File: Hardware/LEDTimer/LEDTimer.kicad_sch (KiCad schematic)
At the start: 36 parts, among them J2 LED, J3 PWR, SW1 SW_Push, SW2 SW_Push, SW3 SW_Push, SW4 SW_BAT, U1 AP7383-36WW7, U2 PIC16F1825, U3 Display_128x64_096_I2C, U4 BCR_421U_E6327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

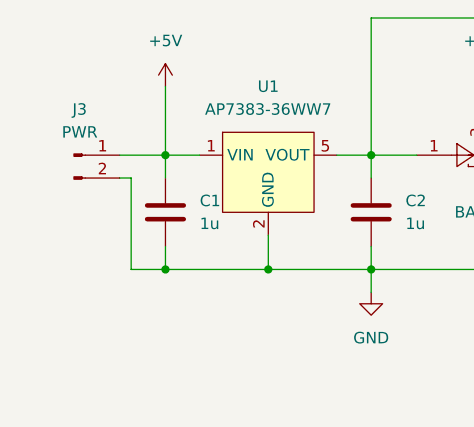
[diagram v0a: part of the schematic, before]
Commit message: PCB: flip the power input connector
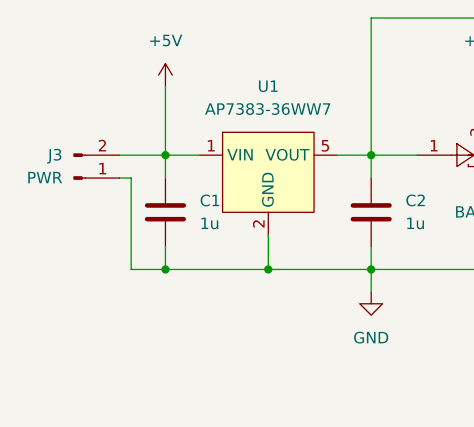
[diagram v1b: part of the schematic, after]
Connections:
- net +5V: now also J3.2 (Pin_2); no longer J3.1 (Pin_1)
- net GND: now also J3.1 (Pin_1); no longer J3.2 (Pin_2)
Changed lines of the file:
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@@
     (pin "3")
   )
-  (symbol (lib_id "Connector:Conn_01x02_Male") (at 20.32 41.91 0) (unit 1)
+  (symbol (lib_id "Connector:Conn_01x02_Male") (at 20.32 44.45 0) (mirror x) (unit 1)
     (in_bom yes) (on_board yes) (fields_autoplaced)
-    (property "Reference" "J3" (id 0) (at 20.955 36.83 0))
-    (property "Value" "PWR" (id 1) (at 20.955 39.37 0))
-    (property "Footprint" "Connector_PinHeader_2.54mm:PinHeader_1x02_P2.54mm_Horizontal" (id 2) (at 20.32 41.91 0)
+    (property "Reference" "J3" (id 0) (at 19.05 41.9099 0)
+      (effects (font (size 1.27 1.27)) (justify right))
+    )
+    (property "Value" "PWR" (id 1) (at 19.05 44.4499 0)
+      (effects (font (size 1.27 1.27)) (justify right))
+    )
+    (property "Footprint" "Connector_PinHeader_2.54mm:PinHeader_1x02_P2.54mm_Horizontal" (id 2) (at 20.32 44.45 0)
       (effects (font (size 1.27 1.27)) hide)
     )
-    (property "Datasheet" "~" (id 3) (at 20.32 41.91 0)
+    (property "Datasheet" "~" (id 3) (at 20.32 44.45 0)
       (effects (font (size 1.27 1.27)) hide)
     )

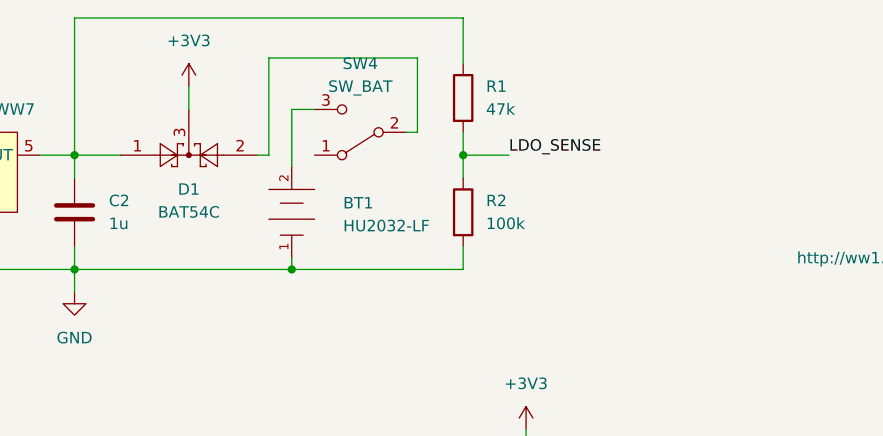
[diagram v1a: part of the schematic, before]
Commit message: PCB: re-purpose the switch as main power switch, add a transistor to LDO_SENSE for protection
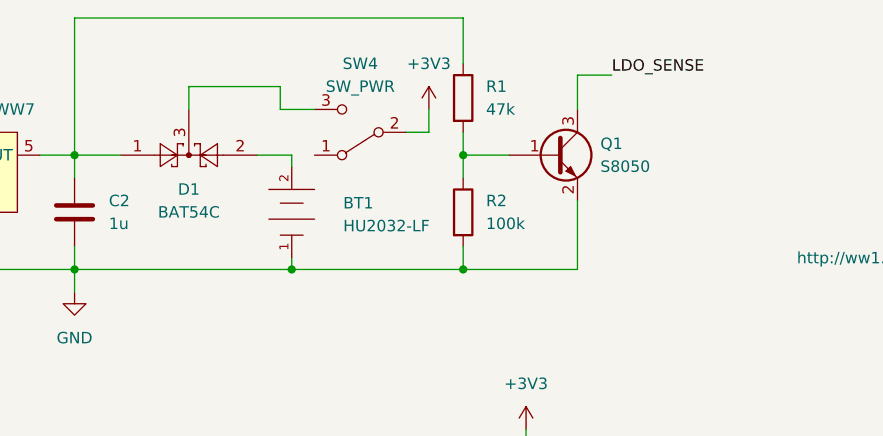
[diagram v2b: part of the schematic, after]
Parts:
- added Q1: S8050, Package_TO_SOT_SMD:SOT-23, symbol Device:Q_NPN_BEC
- SW4: value SW_BAT -> SW_PWR
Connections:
- net +3V3: now also SW4.2 (B); no longer D1.3
- net GND: now also Q1.2 (E)
- net LDO_SENSE: now also Q1.3 (C); no longer R1.2, R2.1
- net at BT1.2 (ANODE): now also D1.2; no longer SW4.3 (C)
- new net: Q1.1 (B), R1.2, R2.1
- new net: D1.3, SW4.3 (C)
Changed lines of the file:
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@@
   (junction (at 194.31 135.89) (diameter 0) (color 0 0 0 0)
   )
+  (junction (at 96.52 54.61) (diameter 0) (color 0 0 0 0)
+  )
   (junction (at 77.47 54.61) (diameter 0) (color 0 0 0 0)
   )
@@
     (stroke (width 0) (type default) (color 0 0 0 0))
   )
-  (wire (pts (xy 74.93 41.91) (xy 73.66 41.91))
+  (wire (pts (xy 73.66 41.91) (xy 77.47 41.91))
     (stroke (width 0) (type default) (color 0 0 0 0))
   )
@@
     (stroke (width 0) (type default) (color 0 0 0 0))
   )
-  (wire (pts (xy 80.01 36.83) (xy 77.47 36.83))
-    (stroke (width 0) (type default) (color 0 0 0 0))
-  )
   (wire (pts (xy 116.205 151.13) (xy 149.225 151.13))
     (stroke (width 0) (type default) (color 0 0 0 0))
@@
     (stroke (width 0) (type default) (color 0 0 0 0))
   )
-  (wire (pts (xy 91.44 31.115) (xy 74.93 31.115))
-    (stroke (width 0) (type default) (color 0 0 0 0))
-  )
   (wire (pts (xy 132.08 76.835) (xy 132.08 83.185))
     (stroke (width 0) (type default) (color 0 0 0 0))
@@
     (stroke (width 0) (type default) (color 0 0 0 0))
   )
-  (wire (pts (xy 77.47 36.83) (xy 77.47 43.18))
-    (stroke (width 0) (type default) (color 0 0 0 0))
-  )
   (wire (pts (xy 88.9 111.76) (xy 86.995 111.76))
     (stroke (width 0) (type default) (color 0 0 0 0))
@@
     (stroke (width 0) (type default) (color 0 0 0 0))
   )
-  (wire (pts (xy 91.44 39.37) (xy 91.44 31.115))
-    (stroke (width 0) (type default) (color 0 0 0 0))
-  )
   (wire (pts (xy 164.465 101.6) (xy 167.005 101.6))
     (stroke (width 0) (type default) (color 0 0 0 0))
@@
     (stroke (width 0) (type default) (color 0 0 0 0))
   )
+  (wire (pts (xy 66.04 34.29) (xy 76.2 34.29))
+    (stroke (width 0) (type default) (color 0 0 0 0))
+  )
   (wire (pts (xy 53.34 41.91) (xy 58.42 41.91))
     (stroke (width 0) (type default) (color 0 0 0 0))
@@
     (stroke (width 0) (type default) (color 0 0 0 0))
   )
+  (wire (pts (xy 109.22 36.83) (xy 109.22 33.02))
+    (stroke (width 0) (type default) (color 0 0 0 0))
+  )
+  (wire (pts (xy 92.71 39.37) (xy 92.71 36.83))
+    (stroke (width 0) (type default) (color 0 0 0 0))
+  )
   (wire (pts (xy 113.665 138.43) (xy 116.205 138.43))
     (stroke (width 0) (type default) (color 0 0 0 0))
@@
     (stroke (width 0) (type default) (color 0 0 0 0))
   )
+  (wire (pts (xy 76.2 36.83) (xy 80.01 36.83))
+    (stroke (width 0) (type default) (color 0 0 0 0))
+  )
   (wire (pts (xy 187.325 85.725) (xy 187.325 111.76))
     (stroke (width 0) (type default) (color 0 0 0 0))
   )
-  (wire (pts (xy 74.93 31.115) (xy 74.93 41.91))
+  (wire (pts (xy 109.22 33.02) (xy 113.03 33.02))
     (stroke (width 0) (type default) (color 0 0 0 0))
   )
@@
     (stroke (width 0) (type default) (color 0 0 0 0))
   )
+  (wire (pts (xy 90.17 39.37) (xy 92.71 39.37))
+    (stroke (width 0) (type default) (color 0 0 0 0))
+  )
   (wire (pts (xy 164.465 104.14) (xy 171.45 104.14))
     (stroke (width 0) (type default) (color 0 0 0 0))
@@
     (stroke (width 0) (type default) (color 0 0 0 0))
   )
+  (wire (pts (xy 77.47 41.91) (xy 77.47 43.18))
+    (stroke (width 0) (type default) (color 0 0 0 0))
+  )
   (wire (pts (xy 193.04 140.97) (xy 194.31 140.97))
     (stroke (width 0) (type default) (color 0 0 0 0))
   )
-  (wire (pts (xy 90.17 39.37) (xy 91.44 39.37))
-    (stroke (width 0) (type default) (color 0 0 0 0))
-  )
   (wire (pts (xy 103.505 76.835) (xy 132.08 76.835))
     (stroke (width 0) (type default) (color 0 0 0 0))
@@
     (stroke (width 0) (type default) (color 0 0 0 0))
   )
+  (wire (pts (xy 109.22 46.99) (xy 109.22 54.61))
+    (stroke (width 0) (type default) (color 0 0 0 0))
+  )
   (wire (pts (xy 173.99 106.68) (xy 173.99 98.425))
     (stroke (width 0) (type default) (color 0 0 0 0))
@@
     (stroke (width 0) (type default) (color 0 0 0 0))
   )
+  (wire (pts (xy 76.2 34.29) (xy 76.2 36.83))
+    (stroke (width 0) (type default) (color 0 0 0 0))
+  )
   (wire (pts (xy 133.985 106.68) (xy 116.205 106.68))
     (stroke (width 0) (type default) (color 0 0 0 0))
@@
   )
   (wire (pts (xy 235.585 102.235) (xy 182.245 102.235))
+    (stroke (width 0) (type default) (color 0 0 0 0))
+  )
+  (wire (pts (xy 109.22 54.61) (xy 96.52 54.61))
     (stroke (width 0) (type default) (color 0 0 0 0))
   )
@@
     (effects (font (size 1.27 1.27)) (justify left bottom))
   )
-  (label "LDO_SENSE" (at 101.6 41.91 0)
+  (label "LDO_SENSE" (at 113.03 33.02 0)
     (effects (font (size 1.27 1.27)) (justify left bottom))
   )
@@
     (pin "2")
     (pin "5")
+  )
+  (symbol (lib_id "Device:Q_NPN_BEC") (at 106.68 41.91 0) (unit 1)
+    (in_bom yes) (on_board yes) (fields_autoplaced)
+    (property "Reference" "Q1" (id 0) (at 111.76 40.6399 0)
+      (effects (font (size 1.27 1.27)) (justify left))
+    )
+    (property "Value" "S8050" (id 1) (at 111.76 43.1799 0)
+      (effects (font (size 1.27 1.27)) (justify left))
+    )
+    (property "Footprint" "Package_TO_SOT_SMD:SOT-23" (id 2) (at 111.76 39.37 0)
+      (effects (font (size 1.27 1.27)) hide)
+    )
+    (property "Datasheet" "https://datasheet.lcsc.com/lcsc/1811101032_HT-Shenzhen-Jinyu-Semicon-S8050_C259988.pdf" (id 3) (at 106.68 41.91 0)
+      (effects (font (size 1.27 1.27)) hide)
+    )
+    (pin "1")
+    (pin "2")
+    (pin "3")
   )
   (symbol (lib_id "Device:R") (at 189.865 81.915 0) (unit 1)
@@
     (pin "1")
   )
-  (symbol (lib_id "power:+3V3") (at 66.04 34.29 0) (unit 1)
-    (in_bom yes) (on_board yes) (fields_autoplaced)
-    (property "Reference" "#PWR03" (id 0) (at 66.04 38.1 0)
-      (effects (font (size 1.27 1.27)) hide)
-    )
-    (property "Value" "+3V3" (id 1) (at 66.04 29.21 0))
-    (property "Footprint" "" (id 2) (at 66.04 34.29 0)
-      (effects (font (size 1.27 1.27)) hide)
-    )
-    (property "Datasheet" "" (id 3) (at 66.04 34.29 0)
+  (symbol (lib_id "power:+3V3") (at 92.71 36.83 0) (unit 1)
+    (in_bom yes) (on_board yes) (fields_autoplaced)
+    (property "Reference" "#PWR03" (id 0) (at 92.71 40.64 0)
+      (effects (font (size 1.27 1.27)) hide)
+    )
+    (property "Value" "+3V3" (id 1) (at 92.71 31.75 0))
+    (property "Footprint" "" (id 2) (at 92.71 36.83 0)
+      (effects (font (size 1.27 1.27)) hide)
+    )
+    (property "Datasheet" "" (id 3) (at 92.71 36.83 0)
       (effects (font (size 1.27 1.27)) hide)
     )
@@
     (in_bom yes) (on_board yes) (fields_autoplaced)
     (property "Reference" "SW4" (id 0) (at 85.09 31.75 0))
-    (property "Value" "SW_BAT" (id 1) (at 85.09 34.29 0))
+    (property "Value" "SW_PWR" (id 1) (at 85.09 34.29 0))
     (property "Footprint" "SPDT Switch:1825232-1" (id 2) (at 85.09 39.37 0)
       (effects (font (size 1.27 1.27)) hide)
@@
       (reference "JP2") (unit 1) (value "OLED2") (footprint "Jumper:SolderJumper-3_P1.3mm_Open_RoundedPad1.0x1.5mm")
     )
+    (path "/8ecc4707-fb83-41b7-ab7c-f7012336c37e"
+      (reference "Q1") (unit 1) (value "S8050") (footprint "Package_TO_SOT_SMD:SOT-23")
+    )
     (path "/c5745adf-2a60-4943-991a-b58822c9fa8c"
       (reference "R1") (unit 1) (value "47k") (footprint "Resistor_SMD:R_0805_2012Metric_Pad1.20x1.40mm_HandSolder")
@@
     )
     (path "/e49a9939-e5f7-4dfe-8005-f25d0240725f"
-      (reference "SW4") (unit 1) (value "SW_BAT") (footprint "SPDT Switch:1825232-1")
+      (reference "SW4") (unit 1) (value "SW_PWR") (footprint "SPDT Switch:1825232-1")
     )
     (path "/da811b11-3f5c-4085-9312-63fa595b7c79"

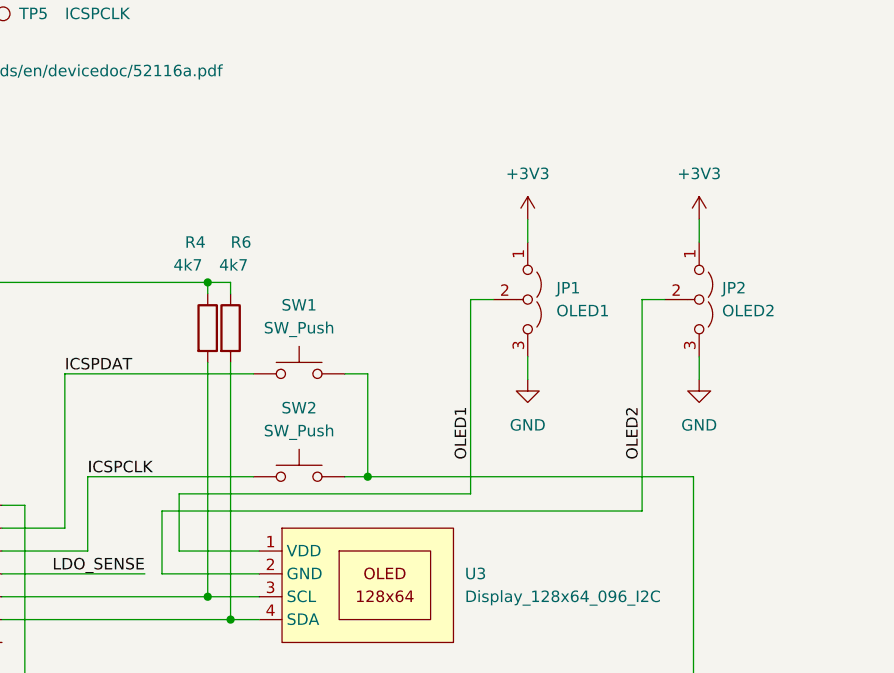
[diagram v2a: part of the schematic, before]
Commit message: PCB: add interactive BOM
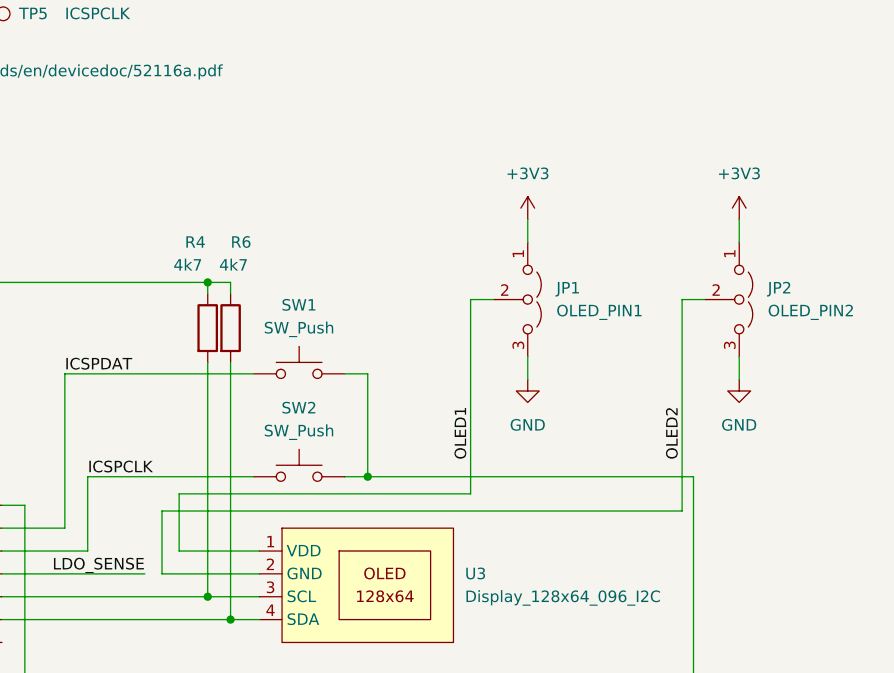
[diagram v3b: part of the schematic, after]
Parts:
- JP1: value OLED1 -> OLED_PIN1
- JP2: value OLED2 -> OLED_PIN2
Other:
- moved on the sheet: JP2
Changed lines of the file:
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@@
     (stroke (width 0) (type default) (color 0 0 0 0))
   )
-  (wire (pts (xy 235.585 78.74) (xy 235.585 102.235))
+  (wire (pts (xy 240.03 78.74) (xy 240.03 102.235))
     (stroke (width 0) (type default) (color 0 0 0 0))
   )
@@
     (stroke (width 0) (type default) (color 0 0 0 0))
   )
-  (wire (pts (xy 238.125 78.74) (xy 235.585 78.74))
+  (wire (pts (xy 242.57 78.74) (xy 240.03 78.74))
     (stroke (width 0) (type default) (color 0 0 0 0))
   )
@@
     (stroke (width 0) (type default) (color 0 0 0 0))
   )
-  (wire (pts (xy 241.935 85.09) (xy 241.935 87.63))
+  (wire (pts (xy 246.38 85.09) (xy 246.38 87.63))
     (stroke (width 0) (type default) (color 0 0 0 0))
   )
@@
     (stroke (width 0) (type default) (color 0 0 0 0))
   )
-  (wire (pts (xy 241.935 69.85) (xy 241.935 72.39))
+  (wire (pts (xy 246.38 69.85) (xy 246.38 72.39))
     (stroke (width 0) (type default) (color 0 0 0 0))
   )
@@
     (stroke (width 0) (type default) (color 0 0 0 0))
   )
-  (wire (pts (xy 235.585 102.235) (xy 182.245 102.235))
+  (wire (pts (xy 240.03 102.235) (xy 182.245 102.235))
     (stroke (width 0) (type default) (color 0 0 0 0))
   )
@@
     (effects (font (size 1.27 1.27)) (justify left bottom))
   )
-  (label "OLED2" (at 235.585 96.52 90)
+  (label "OLED2" (at 240.03 96.52 90)
     (effects (font (size 1.27 1.27)) (justify left bottom))
   )
@@
     )
   )
-  (symbol (lib_id "Jumper:Jumper_3_Open") (at 241.935 78.74 270) (unit 1)
-    (in_bom yes) (on_board yes) (fields_autoplaced)
-    (property "Reference" "JP2" (id 0) (at 244.475 77.4699 90)
-      (effects (font (size 1.27 1.27)) (justify left))
-    )
-    (property "Value" "OLED2" (id 1) (at 244.475 80.0099 90)
-      (effects (font (size 1.27 1.27)) (justify left))
-    )
-    (property "Footprint" "Jumper:SolderJumper-3_P1.3mm_Open_RoundedPad1.0x1.5mm" (id 2) (at 241.935 78.74 0)
-      (effects (font (size 1.27 1.27)) hide)
-    )
-    (property "Datasheet" "~" (id 3) (at 241.935 78.74 0)
+  (symbol (lib_id "Jumper:Jumper_3_Open") (at 246.38 78.74 270) (unit 1)
+    (in_bom yes) (on_board yes) (fields_autoplaced)
+    (property "Reference" "JP2" (id 0) (at 249.555 77.4699 90)
+      (effects (font (size 1.27 1.27)) (justify left))
+    )
+    (property "Value" "OLED_PIN2" (id 1) (at 249.555 80.0099 90)
+      (effects (font (size 1.27 1.27)) (justify left))
+    )
+    (property "Footprint" "Jumper:SolderJumper-3_P1.3mm_Open_RoundedPad1.0x1.5mm" (id 2) (at 246.38 78.74 0)
+      (effects (font (size 1.27 1.27)) hide)
+    )
+    (property "Datasheet" "~" (id 3) (at 246.38 78.74 0)
       (effects (font (size 1.27 1.27)) hide)
     )
@@
     )
   )
-  (symbol (lib_id "power:+3V3") (at 241.935 69.85 0) (unit 1)
-    (in_bom yes) (on_board yes) (fields_autoplaced)
-    (property "Reference" "#PWR0104" (id 0) (at 241.935 73.66 0)
-      (effects (font (size 1.27 1.27)) hide)
-    )
-    (property "Value" "+3V3" (id 1) (at 241.935 64.77 0))
-    (property "Footprint" "" (id 2) (at 241.935 69.85 0)
-      (effects (font (size 1.27 1.27)) hide)
-    )
-    (property "Datasheet" "" (id 3) (at 241.935 69.85 0)
+  (symbol (lib_id "power:+3V3") (at 246.38 69.85 0) (unit 1)
+    (in_bom yes) (on_board yes) (fields_autoplaced)
+    (property "Reference" "#PWR0104" (id 0) (at 246.38 73.66 0)
+      (effects (font (size 1.27 1.27)) hide)
+    )
+    (property "Value" "+3V3" (id 1) (at 246.38 64.77 0))
+    (property "Footprint" "" (id 2) (at 246.38 69.85 0)
+      (effects (font (size 1.27 1.27)) hide)
+    )
+    (property "Datasheet" "" (id 3) (at 246.38 69.85 0)
       (effects (font (size 1.27 1.27)) hide)
     )
@@
     (pin "2")
   )
-  (symbol (lib_id "power:GND") (at 241.935 87.63 0) (unit 1)
-    (in_bom yes) (on_board yes) (fields_autoplaced)
-    (property "Reference" "#PWR0102" (id 0) (at 241.935 93.98 0)
-      (effects (font (size 1.27 1.27)) hide)
-    )
-    (property "Value" "GND" (id 1) (at 241.935 92.71 0))
-    (property "Footprint" "" (id 2) (at 241.935 87.63 0)
-      (effects (font (size 1.27 1.27)) hide)
-    )
-    (property "Datasheet" "" (id 3) (at 241.935 87.63 0)
+  (symbol (lib_id "power:GND") (at 246.38 87.63 0) (unit 1)
+    (in_bom yes) (on_board yes) (fields_autoplaced)
+    (property "Reference" "#PWR0102" (id 0) (at 246.38 93.98 0)
+      (effects (font (size 1.27 1.27)) hide)
+    )
+    (property "Value" "GND" (id 1) (at 246.38 92.71 0))
+    (property "Footprint" "" (id 2) (at 246.38 87.63 0)
+      (effects (font (size 1.27 1.27)) hide)
+    )
+    (property "Datasheet" "" (id 3) (at 246.38 87.63 0)
       (effects (font (size 1.27 1.27)) hide)
     )
@@
       (effects (font (size 1.27 1.27)) (justify left))
     )
-    (property "Value" "OLED1" (id 1) (at 226.06 80.0099 90)
+    (property "Value" "OLED_PIN1" (id 1) (at 226.06 80.0099 90)
       (effects (font (size 1.27 1.27)) (justify left))
     )
@@
     )
     (path "/ca50989c-806e-4138-b3ff-f2b2f96652a0"
-      (reference "JP1") (unit 1) (value "OLED1") (footprint "Jumper:SolderJumper-3_P1.3mm_Open_RoundedPad1.0x1.5mm")
+      (reference "JP1") (unit 1) (value "OLED_PIN1") (footprint "Jumper:SolderJumper-3_P1.3mm_Open_RoundedPad1.0x1.5mm")
     )
     (path "/3f772120-8435-4569-9ddb-0201d4f94057"
-      (reference "JP2") (unit 1) (value "OLED2") (footprint "Jumper:SolderJumper-3_P1.3mm_Open_RoundedPad1.0x1.5mm")
+      (reference "JP2") (unit 1) (value "OLED_PIN2") (footprint "Jumper:SolderJumper-3_P1.3mm_Open_RoundedPad1.0x1.5mm")
     )
     (path "/8ecc4707-fb83-41b7-ab7c-f7012336c37e"
